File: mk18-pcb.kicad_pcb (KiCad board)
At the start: 2 copper layers, 121.5 x 66 mm, 48 parts

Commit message: jan4 updates
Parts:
- removed BOOST-CONVERT1: SRV0504, ct-kicad:SOT-23-6_L2.9-W1.6-P0.95-LS2.8-BL
- added U2: AZC199-04S-MS, ct-kicad:TSOT-23-6_L2.9-W1.6-P0.95-LS2.8-BL, F.Cu at (191.4, 82.7)
- moved H2 52.6 mm to (177.5, 74.1)
- moved PWM1 45.8 mm to (201.2, 125.8), turned to 90 degrees
- moved ROW2 41.1 mm to (141.5, 112.6), turned to 180 degrees
- moved LED-MACRO1 40.5 mm to (179.8, 99.6), turned to -90 degrees
- moved H5 36.1 mm to (218.4, 75.3)
- moved RESET1 35.8 mm to (214.3, 102.0), turned to 90 degrees
- moved LED-FAL2 26.7 mm to (193.4, 99.5), turned to -90 degrees
- moved COL2 25.2 mm to (124.1, 88.5), turned to 0 degrees
- moved LED-FAL1 22.9 mm to (185.9, 102.0)
- moved LED-IND1 21.6 mm to (199.5, 102.0), turned to 90 degrees
- moved IND1 18.5 mm to (194.0, 125.8)
- moved R7 18.4 mm to (138.7, 74.5)
- moved COL_CS_MOS1 18.4 mm to (142.5, 74.6)
- moved REG-ROW2 16.9 mm to (107.1, 121.6)
- moved C4 15.1 mm to (112.8, 124.7)
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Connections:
- PWM1 pad 1: +3V3 -> GND
- PWM1 pad 6: unconnected-(PWM1-Pin_6-Pad6) -> +3V3
- PWM1 pad 7: GND -> unconnected-(PWM1-Pin_7-Pad7)
- SCREEN1 pad A4: VCC -> Serial_VBUS
- SCREEN1 pad A9: VCC -> Serial_VBUS
- SCREEN1 pad B4: VCC -> Serial_VBUS
- SCREEN1 pad B9: VCC -> Serial_VBUS
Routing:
- net SPI1_CLK: track 116.7 -> 237.5 mm, vias 9 -> 12
- net SPI1_MISO: track 73.6 -> 188.5 mm, vias 4 -> 6
- net GND: track 163.2 -> 56.3 mm, vias 45 -> 99
- net PMW_CS: track 18.9 -> 98.2 mm, vias 3 -> 0
- net SPI1_MOSI: track 50.0 -> 125.0 mm, vias 3 -> 6
- net LED_FAL1_DI: track 159.7 -> 86.8 mm, vias 7 -> 5
- net +3V3: track 228.0 -> 296.8 mm, vias 12 -> 22
- net LED_KEYS_DO: track 24.3 -> 90.4 mm, vias 2 -> 8
- net reset: track 9.68 -> 50.4 mm, vias 0 -> 5
- net row6: track 9.99 -> 50.3 mm, vias 4 -> 1
- net LED_KEYS_DI: track 113.8 -> 75.7 mm
- net ROW_CS: track 46.2 -> 83.9 mm
- net row1: track 18.5 -> 53.8 mm, vias 4 -> 2
- net VCC: track 291.9 -> 256.8 mm, vias 15 -> 21
- net row2: track 12.4 -> 38.2 mm, vias 2 -> 1
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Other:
- board size 121.5 x 66 mm -> 128.2 x 66 mm
- board text added: "F1 > F2"
- board text added: "F2 > IN"
- board text added: "K > F1"
- board text added: "LED BYPASS"
- board text added: "PERIPHERALS"

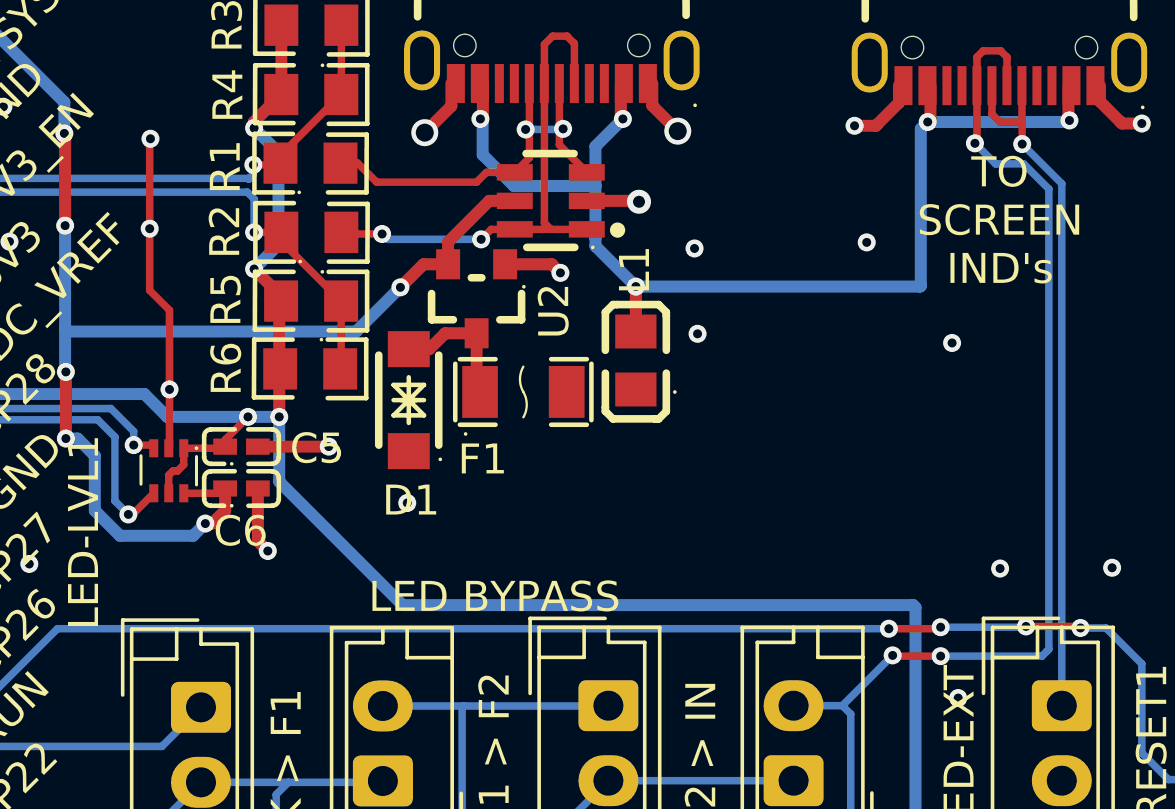
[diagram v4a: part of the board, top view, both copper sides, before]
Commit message: added bypass for safeties
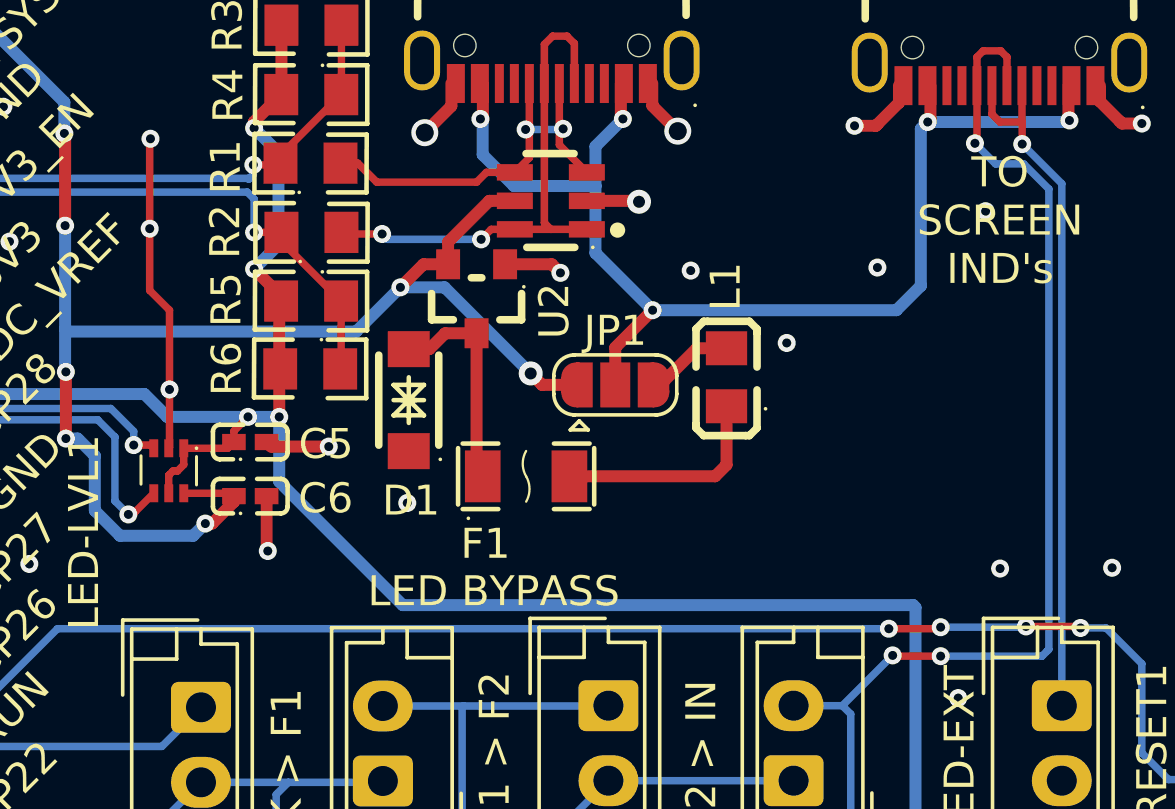
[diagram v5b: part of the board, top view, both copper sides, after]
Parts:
- added JP1: SolderJumper_3_Open, Jumper:SolderJumper-3_P1.3mm_Open_RoundedPad1.0x1.5mm, F.Cu at (193.6, 88.8)
- moved L1 3.07 mm to (197.3, 88.6)
- moved F1 2.81 mm to (190.6, 91.9)
- moved C6 0.39 mm to (181.4, 92.5)
- moved C5 0.33 mm to (181.4, 90.7)
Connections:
- L1 pad 2: Serial_VBUS -> Net-(JP1-B)
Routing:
- net Net-(F1-Pad2): track 0.00 -> 7.35 mm
- net VCC: track 256.8 -> 264.2 mm, vias 21 -> 22
- net Net-(JP1-B): track 0.00 -> 2.91 mm
- net Net-(D1-A): track 4.48 -> 7.33 mm
- net Serial_VBUS: track 38.1 -> 40.4 mm
- net GND: track 56.3 -> 55.7 mm

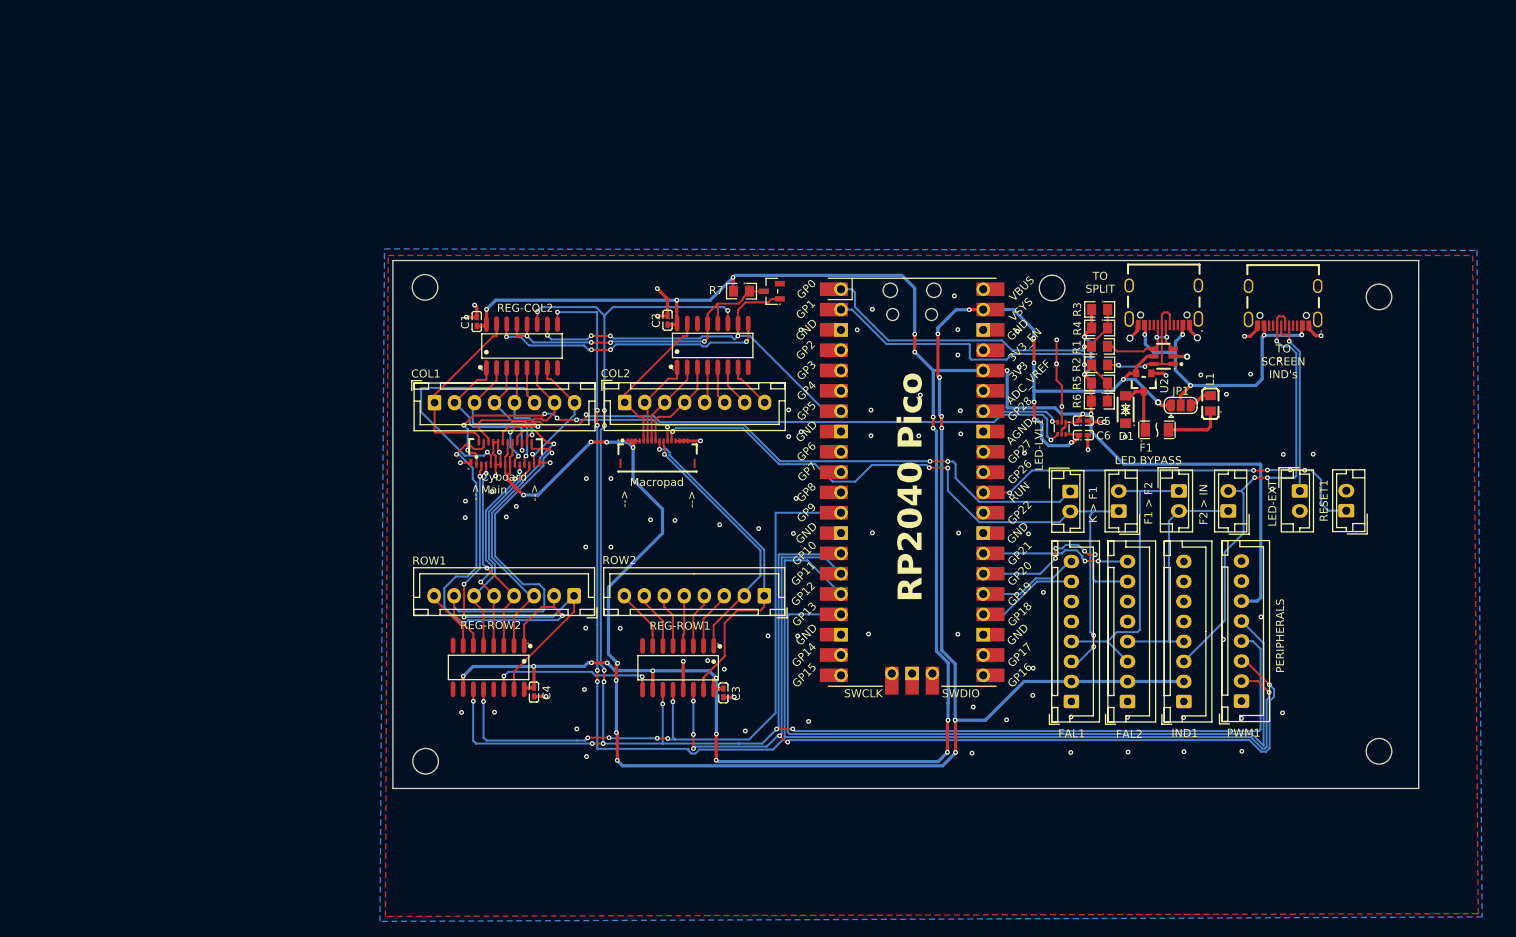
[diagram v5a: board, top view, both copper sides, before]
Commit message: prior to removing pull-up resistors on comms
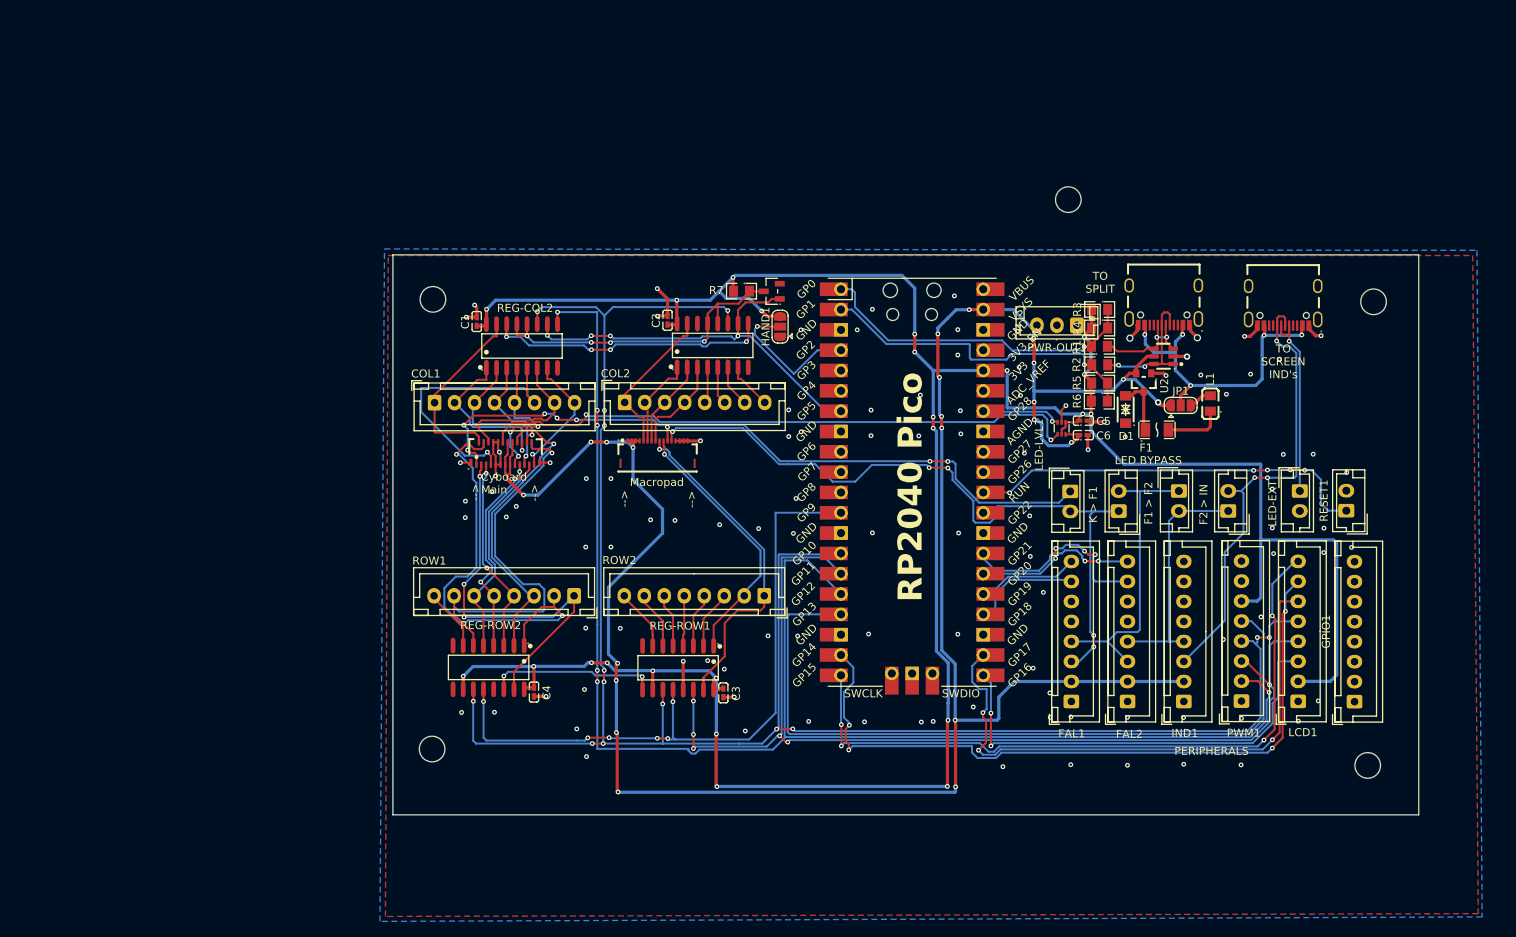
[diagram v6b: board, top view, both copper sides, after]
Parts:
- added GPIO1: Conn_01x08_Socket, Connector_JST:JST_XH_B8B-XH-A_1x08_P2.50mm_Vertical, F.Cu at (215.3, 125.8)
- added HAND1: SolderJumper_3_Open, Jumper:SolderJumper-3_P1.3mm_Open_RoundedPad1.0x1.5mm, F.Cu at (143.5, 79.0)
- added LCD1: Conn_01x08_Socket, Connector_JST:JST_XH_B8B-XH-A_1x08_P2.50mm_Vertical, F.Cu at (208.3, 125.8)
- added PWR-OUT1: Conn_01x03_Socket, Connector_JST:JST_EH_B3B-EH-A_1x03_P2.50mm_Vertical, F.Cu at (180.6, 78.8)
- moved H2 11.2 mm to (179.6, 63.1)
- moved H4 2.27 mm to (217.0, 133.8)
- moved H1 1.80 mm to (100.1, 75.6)
- moved H3 1.73 mm to (100.0, 131.8)
- moved H5 0.92 mm to (217.7, 75.9)
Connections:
- PICO1 pad 10: unconnected-(PICO1-GPIO7-Pad10) -> GPIO7
- PICO1 pad 11: unconnected-(PICO1-GPIO8-Pad11) -> GPIO8
- PICO1 pad 19: unconnected-(PICO1-GPIO14-Pad19) -> LCD_DC
- PICO1 pad 20: unconnected-(PICO1-GPIO15-Pad20) -> LCD_BL
- PICO1 pad 21: unconnected-(PICO1-GPIO16-Pad21) -> LCD_CS
- PICO1 pad 22: unconnected-(PICO1-GPIO17-Pad22) -> LCD_RST
- PICO1 pad 29: unconnected-(PICO1-GPIO22-Pad29) -> GPIO22
- PICO1 pad 31: unconnected-(PICO1-GPIO26_ADC0-Pad31) -> GPIO26
- PICO1 pad 32: unconnected-(PICO1-GPIO27_ADC1-Pad32) -> GPIO27
- PICO1 pad 4: unconnected-(PICO1-GPIO2-Pad4) -> Net-(HAND1-C)
- PICO1 pad 5: unconnected-(PICO1-GPIO3-Pad5) -> GPIO3
- PICO1 pad 6: unconnected-(PICO1-GPIO4-Pad6) -> GPIO4
- PICO1 pad 9: unconnected-(PICO1-GPIO6-Pad9) -> GPIO6
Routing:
- net LCD_DC: track 0.00 -> 90.5 mm, vias 0 -> 4
- net LCD_BL: track 0.00 -> 87.5 mm, vias 0 -> 4
- net LCD_RST: track 0.00 -> 72.2 mm, vias 0 -> 3
- net LCD_CS: track 0.00 -> 56.1 mm, vias 0 -> 2
- net +3V3: track 296.8 -> 344.0 mm, vias 22 -> 23
- net Net-(HAND1-C): track 0.00 -> 18.1 mm, vias 0 -> 1
- net VCC: track 264.2 -> 273.6 mm, vias 22 -> 23
- net GND: track 55.7 -> 47.4 mm, vias 99 -> 108
- net SPI1_CLK: track 237.5 -> 244.4 mm, vias 12 -> 14
- net SPI1_MOSI: track 125.0 -> 130.6 mm
- net SPI1_MISO: track 188.5 -> 185.3 mm
- net fal2-r2: track 19.0 -> 21.4 mm
- net PMW_CS: track 98.2 -> 95.8 mm
- net LED_FAL1_DI: track 86.8 -> 88.4 mm
- net fal1-r1: track 12.7 -> 14.1 mm
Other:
- board size 128.2 x 66 mm -> 128.2 x 70 mm

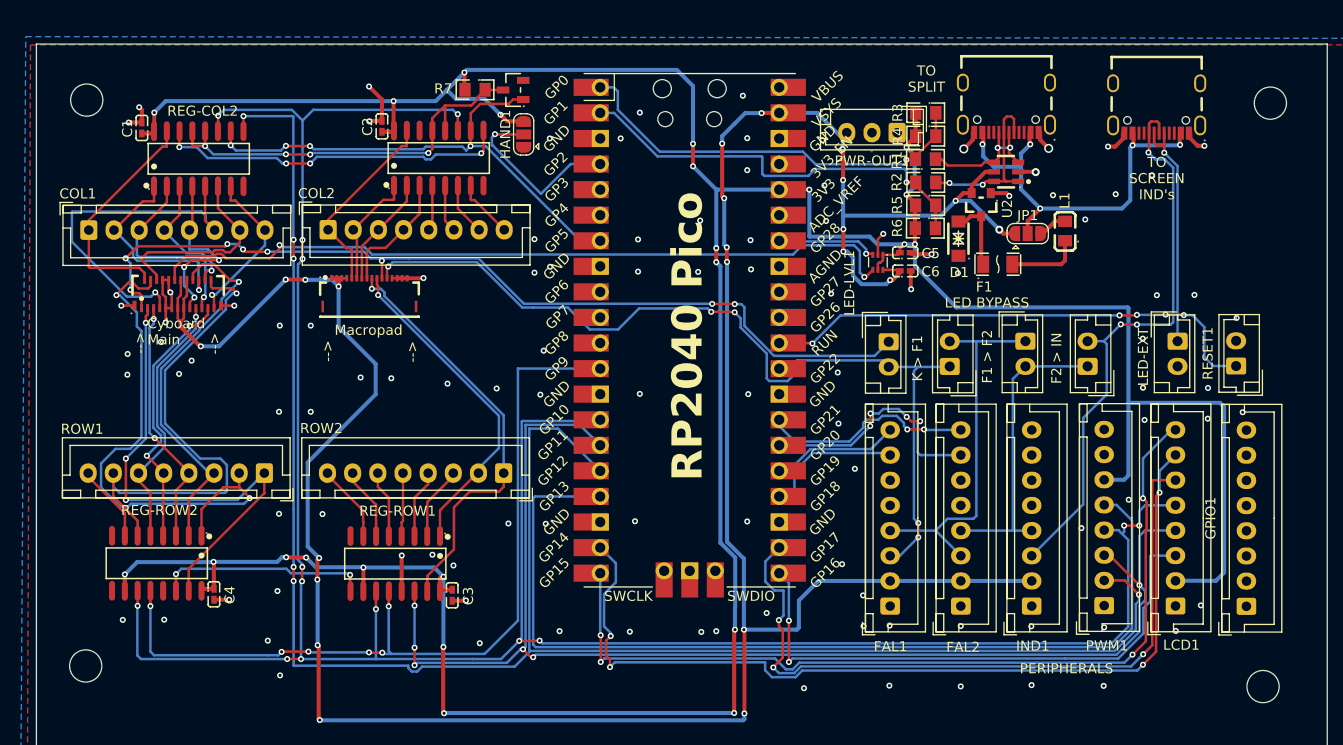
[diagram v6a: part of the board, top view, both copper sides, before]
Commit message: jan6 updates, added 5way, moved all vias off silkscreen, added breakouts
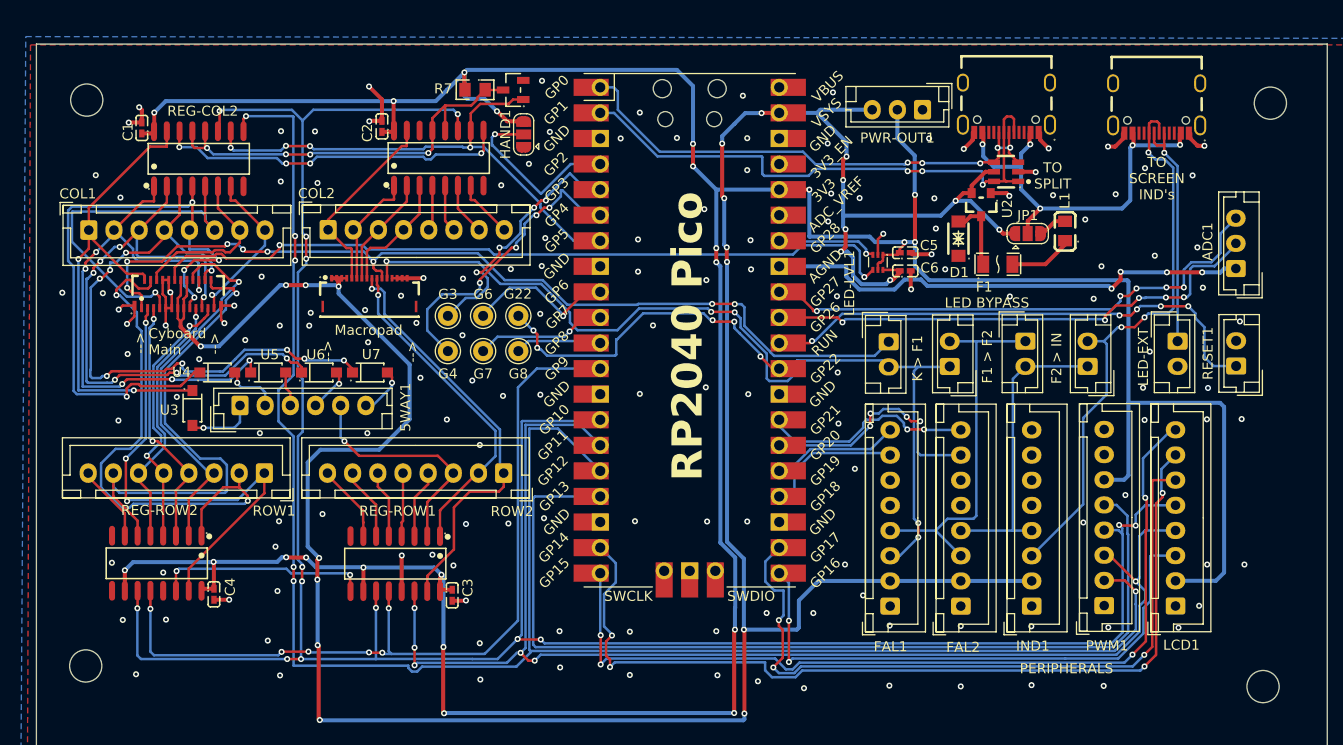
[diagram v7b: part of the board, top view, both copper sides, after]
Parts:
- removed GPIO1: Conn_01x08_Socket, Connector_JST:JST_XH_B8B-XH-A_1x08_P2.50mm_Vertical
- removed R1, R2: 120, ct-kicad:R0805
- removed R3, R6: RK73H2ATTD9101F, ct-kicad:R0805
- removed R4, R5: WR08X1200FTL, ct-kicad:R0805
- added 5WAY1: Conn_01x06_Socket, Connector_JST:JST_EH_B6B-EH-A_1x06_P2.50mm_Vertical, F.Cu at (115.3, 105.9)
- added ADC1: Conn_01x03_Socket, Connector_JST:JST_EH_B3B-EH-A_1x03_P2.50mm_Vertical, F.Cu at (214.3, 92.3)
- added G22: Conn_01x01_Socket, Connector_Pin:Pin_D1.0mm_L10.0mm, F.Cu at (143.0, 97.0)
- added G3: Conn_01x01_Socket, Connector_Pin:Pin_D1.0mm_L10.0mm, F.Cu at (136.0, 97.0)
- added G4: Conn_01x01_Socket, Connector_Pin:Pin_D1.0mm_L10.0mm, F.Cu at (136.0, 100.5)
- added G6: Conn_01x01_Socket, Connector_Pin:Pin_D1.0mm_L10.0mm, F.Cu at (139.5, 97.0)
- added G7: Conn_01x01_Socket, Connector_Pin:Pin_D1.0mm_L10.0mm, F.Cu at (139.5, 100.5)
- added G8: Conn_01x01_Socket, Connector_Pin:Pin_D1.0mm_L10.0mm, F.Cu at (143.0, 100.5)
- added U3: 1N4148W_C81598, ct-kicad:SOD-123F_L2.7-W1.6-LS3.8-RD, F.Cu at (110.6, 106.2)
- added U4: 1N4148W_C81598, ct-kicad:SOD-123F_L2.7-W1.6-LS3.8-RD, F.Cu at (113.1, 102.6)
- added U5: 1N4148W_C81598, ct-kicad:SOD-123F_L2.7-W1.6-LS3.8-RD, F.Cu at (118.2, 102.6)
- added U6: 1N4148W_C81598, ct-kicad:SOD-123F_L2.7-W1.6-LS3.8-RD, F.Cu at (123.2, 102.6)
- added U7: 1N4148W_C81598, ct-kicad:SOD-123F_L2.7-W1.6-LS3.8-RD, F.Cu at (128.3, 102.6)
- moved PWR-OUT1 3.40 mm to (183.2, 76.5)
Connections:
- PICO1 pad 33: unconnected-(PICO1-AGND-Pad33) -> AGND
- SPLIT-USB1 pad A6: Split_Comms_TX-A6 -> Split_Comms_TX
- SPLIT-USB1 pad A7: Split_Comms_RX-A7 -> Split_Comms_RX
- SPLIT-USB1 pad B6: Split_Comms_TX-A6 -> Split_Comms_TX
- SPLIT-USB1 pad B7: Split_Comms_RX-A7 -> Split_Comms_RX
- U2 pad 1: Split_Comms_RX-A7 -> Split_Comms_RX
- U2 pad 3: Split_Comms_TX-A6 -> Split_Comms_TX
- U2 pad 4: Split_Comms_TX-A6 -> Split_Comms_TX
- U2 pad 6: Split_Comms_RX-A7 -> Split_Comms_RX
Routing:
- net GPIO27: track 0.00 -> 52.5 mm, vias 0 -> 5
- net GPIO26: track 0.00 -> 50.7 mm, vias 0 -> 5
- net AGND: track 0.00 -> 49.0 mm, vias 0 -> 4
- net col3: track 13.3 -> 62.0 mm, vias 1 -> 9
- net col4: track 18.2 -> 63.2 mm, vias 3 -> 5
- net col2: track 19.9 -> 61.5 mm, vias 1 -> 7
- net col1: track 21.3 -> 57.1 mm, vias 1 -> 6
- net GPIO22: track 0.00 -> 33.8 mm, vias 0 -> 5
- net GPIO4: track 0.00 -> 30.0 mm, vias 0 -> 4
- net col0: track 23.4 -> 49.9 mm, vias 0 -> 2
- net GPIO3: track 0.00 -> 25.7 mm, vias 0 -> 4
- net Split_Comms_RX-A7: track 17.2 -> 0.00 mm, vias 2 -> 0
- net row10: track 7.33 -> 23.3 mm, vias 0 -> 1
- net GPIO6: track 0.00 -> 15.3 mm, vias 0 -> 1
- net Split_Comms_TX-A6: track 14.2 -> 0.00 mm, vias 2 -> 0
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
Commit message: really close now maybe kinda
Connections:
- FAL1 pad 5: fal1-row -> row11
- FAL1 pad 6: fal1-col -> col0
- FAL2 pad 5: fal2-row -> row11
- FAL2 pad 6: fal2-col -> col1
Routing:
- net col1: track 57.1 -> 187.5 mm, vias 6 -> 16
- net col0: track 49.9 -> 176.9 mm, vias 2 -> 9
- net row11: track 6.82 -> 102.5 mm, vias 0 -> 7
- net +3V3: track 345.9 -> 355.6 mm, vias 22 -> 24
- net row1: track 54.3 -> 45.2 mm
- net SPI1_MISO: track 186.4 -> 179.4 mm
- net SPI1_MOSI: track 130.8 -> 124.8 mm
- net LCD_DC: track 90.9 -> 93.4 mm
- net col3: track 62.0 -> 60.2 mm
- net LCD_RST: track 72.3 -> 74.0 mm
- net LCD_CS: track 56.1 -> 57.8 mm
- net SPI1_CLK: track 245.2 -> 243.6 mm
- net GND: track 52.1 -> 53.7 mm, vias 156 -> 168
- net LED_FAL1_DI: track 89.6 -> 91.1 mm
- net PMW_CS: track 95.4 -> 93.9 mm
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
